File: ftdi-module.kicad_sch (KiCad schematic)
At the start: 60 parts, among them U1 AP62301_TSOT, U2 FT4232H_VQFN, U3 AP62301_TSOT, Y1 Resonator_12MHz_ABM8G

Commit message: Implement changes suggested in schematic review
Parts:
- removed C15, C17, C19, C6, C9: C_100n_0402, antmicro-footprints:C_0402_1005Metric, symbol antmicroCapacitors0402:C_100n_0402
- removed C2, C4: C_4u7_0402, antmicro-footprints:C_0402_1005Metric, symbol antmicroCapacitors0402:C_4u7_0402
- removed FB1, FB2: FB_600Z_0.5A_Murata-BLM18AG_0603, antmicro-footprints:FB_0603_1608Metric, symbol antmicroFerriteBeadsandChips:FB_600Z_0.5A_Murata-BLM18AG_0603
- removed R15: R_33k2_0402, antmicro-footprints:R_0402_1005Metric, symbol antmicroResistors0402:R_33k2_0402
- removed R16, R7: R_10k_0402, antmicro-footprints:R_0402_1005Metric, symbol antmicroResistors0402:R_10k_0402
- removed R6: R_52k3_0402, antmicro-footprints:R_0402_1005Metric, symbol antmicroResistors0402:R_52k3_0402
- removed TP6: TP_1mm_SMD, antmicro-footprints:TP_SMD_1mm, symbol antmicroTestPoints:TP_1mm_SMD
- added C?: C_3u3_0402, antmicro-footprints:C_0402_1005Metric, symbol antmicroCapacitors0402:C_3u3_0402
- added C? (x2): C_100n_0402, antmicro-footprints:C_0402_1005Metric, symbol antmicroCapacitors0402:C_100n_0402
- added C? (x2): C_4u7_0402, antmicro-footprints:C_0402_1005Metric, symbol antmicroCapacitors0402:C_4u7_0402
- added FB? (x2): FB_600Z_0.5A_Murata-BLM18AG_0603, antmicro-footprints:FB_0603_1608Metric, symbol antmicroFerriteBeadsandChips:FB_600Z_0.5A_Murata-BLM18AG_0603
- added R? (x2): R_0R_0402, antmicro-footprints:R_0402_1005Metric, symbol antmicroResistors0402:R_0R_0402
- added R?: R_6k34_0402, antmicro-footprints:R_0402_1005Metric, symbol antmicroResistors0402:R_6k34_0402
- added R? (x2): R_2k_0402, antmicro-footprints:R_0402_1005Metric, symbol antmicroResistors0402:R_2k_0402
- added R?: R_10k7_0402, antmicro-footprints:R_0402_1005Metric, symbol antmicroResistors0402:R_10k7_0402
- C12, R17, R18, R9: DNP (none) -> DNP
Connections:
- net +3V3: now also FB?.1, FB?.1
- net 1V8_FT: now also C?.2
- net FTDI_VPHY: now also C?.2, C?.2, FB?.2
- net FTDI_VPLL: now also C?.2, C?.2, FB?.2
- net GND: now also C?.1, C?.1, C?.1, C?.1, C?.1, R?.2, R?.2
- net SCL: now also R?.2; no longer U2.12 (ADBUS0)
- net SDA: now also R?.2; no longer U2.14 (ADBUS2)
- net at U3.4 (FB): now also R?.1, R?.1
- net at C22.2, C23.2, FB4.1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: now also R?.2
- net at C10.2, C11.2, FB3.1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: now also R?.2
- net at U1.4 (FB): now also R?.1, R?.1
- net SDA_FTDI_2: no longer names the net of R9.1, U2.13 (ADBUS1)
- net USB_D+ renamed USB_BACKPLANE_D+
- net USB_D- renamed USB_BACKPLANE_D-
- net WP: no longer names the net of U2.15 (ADBUS3)
- new net: R?.1, U2.12 (ADBUS0)
- new net: R?.1, U2.14 (ADBUS2)
- no-connect marks 32 -> 33
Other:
- note added: "Values for feedback resitors have been divided by 5 (comparing to datasheet) to eliminate converter failure caused by accidential touch"
- company: (none) -> Antmicro Ltd
- moved on the sheet: C1, C10, C11, C12, C14, C16, C18, C20, C21, C22, C23, C5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

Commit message: 2nd part of review changes
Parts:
- added C15, C17: C_100n_0402, antmicro-footprints:C_0402_1005Metric, symbol antmicroCapacitors0402:C_100n_0402
- C12: DNP DNP -> (none)
- gave numbers to parts that had none: 13
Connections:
- net 1V8_FT: now also C15.2, C17.2
- net GND: now also C15.1, C17.1
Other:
- moved on the sheet: C19

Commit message: Cleaning ERC on schematic
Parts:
- removed FB3, FB4: BLM21SN300SZ1D, antmicro-footprints:FB_0805_2012Metric, symbol antmicroFerriteBeadsandChips:BLM21SN300SZ1D
- added FB3, FB4: FB_30Z_8.5A_Murata-BLM21SN_0805, antmicro-footprints:FB_0805_2012Metric, symbol antmicroFerriteBeadsandChips:FB_30Z_8.5A_Murata-BLM21SN_0805
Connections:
- net +3V3: now also FB4.2
- net +5V: now also FB3.2
- net at C22.2, C23.2, L2.2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: now also FB4.1
- net at C10.2, C11.2, L1.2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: now also FB3.1

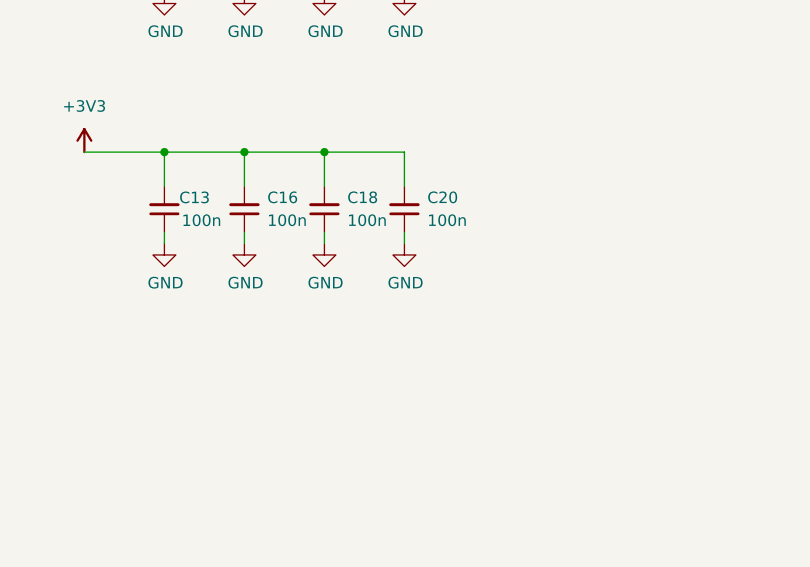
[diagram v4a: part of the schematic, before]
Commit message: Fix possible ERC errors
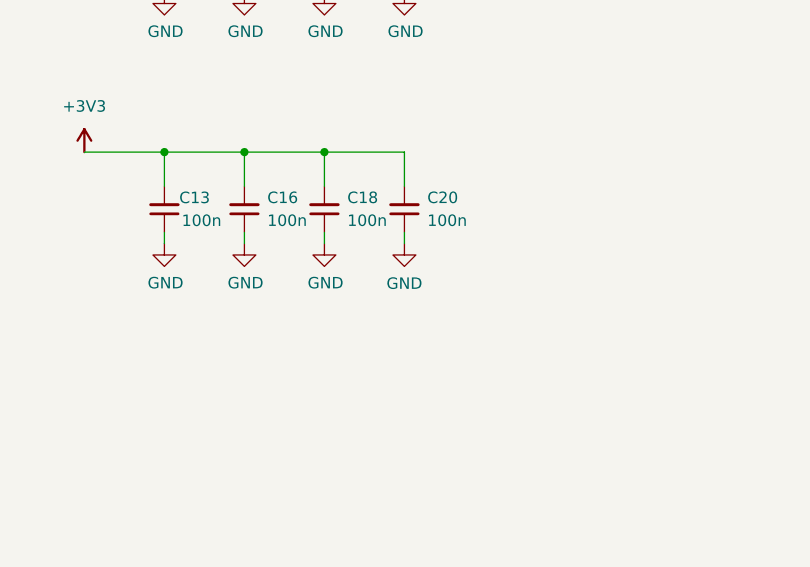
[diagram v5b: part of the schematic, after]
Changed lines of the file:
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@@
     (pin "2")
   )
-  (symbol (lib_id "antmicropower:GND") (at 237.49 133.35 0) (unit 1)
+  (symbol (lib_name "GND_4") (lib_id "antmicropower:GND") (at 237.49 133.35 0) (unit 1)
     (in_bom yes) (on_board yes)
-    (property "Reference" "#PWR035" (id 0) (at 237.49 139.7 0)
-      (effects (font (size 1.27 1.27)) hide)
+    (property "Reference" "#PWR0416" (id 0) (at 246.38 135.89 0)
+      (effects (font (size 1.27 1.27) (thickness 0.15)) (justify left bottom) hide)
     )
-    (property "Value" "GND" (id 1) (at 237.617 137.7442 0))
-    (property "Footprint" "" (id 2) (at 237.49 133.35 0)
-      (effects (font (size 1.27 1.27)) hide)
+    (property "Value" "GND" (id 1) (at 237.49 137.795 0)
+      (effects (font (size 1.27 1.27) (thickness 0.15)))
     )
-    (property "Datasheet" "" (id 3) (at 237.49 133.35 0)
-      (effects (font (size 1.27 1.27)) hide)
+    (property "Footprint" "" (id 2) (at 246.38 140.97 0)
+      (effects (font (size 1.27 1.27) (thickness 0.15)) (justify left bottom) hide)
+    )
+    (property "Datasheet" "" (id 3) (at 246.38 146.05 0)
+      (effects (font (size 1.27 1.27) (thickness 0.15)) (justify left bottom) hide)
+    )
+    (property "Author" "Antmicro" (id 4) (at 246.38 140.97 0)
+      (effects (font (size 1.27 1.27) (thickness 0.15)) (justify left bottom) hide)
+    )
+    (property "License" "Apache-2.0" (id 5) (at 246.38 143.51 0)
+      (effects (font (size 1.27 1.27) (thickness 0.15)) (justify left bottom) hide)
     )
     (pin "1")

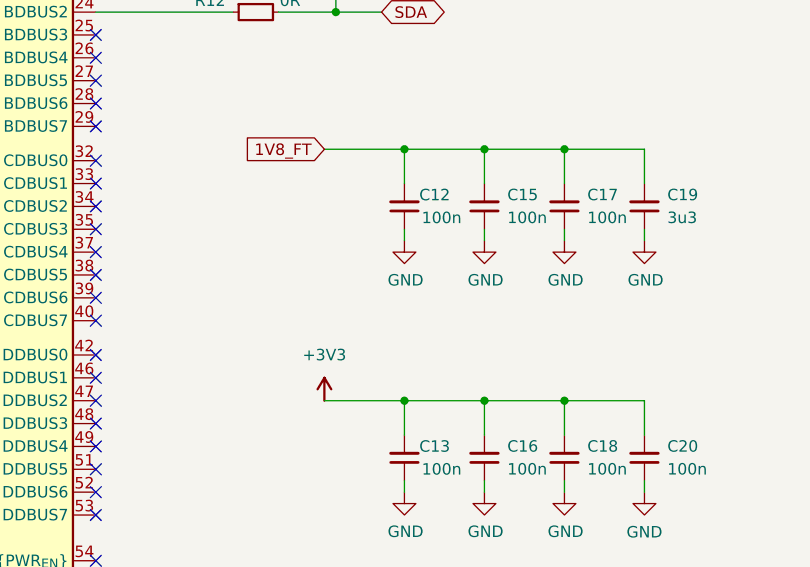
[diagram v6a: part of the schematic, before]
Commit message: Fix ERC errors
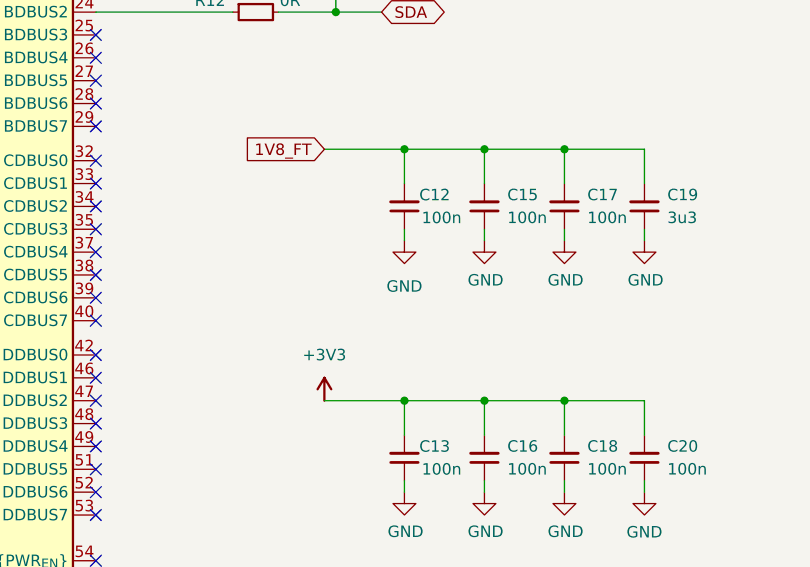
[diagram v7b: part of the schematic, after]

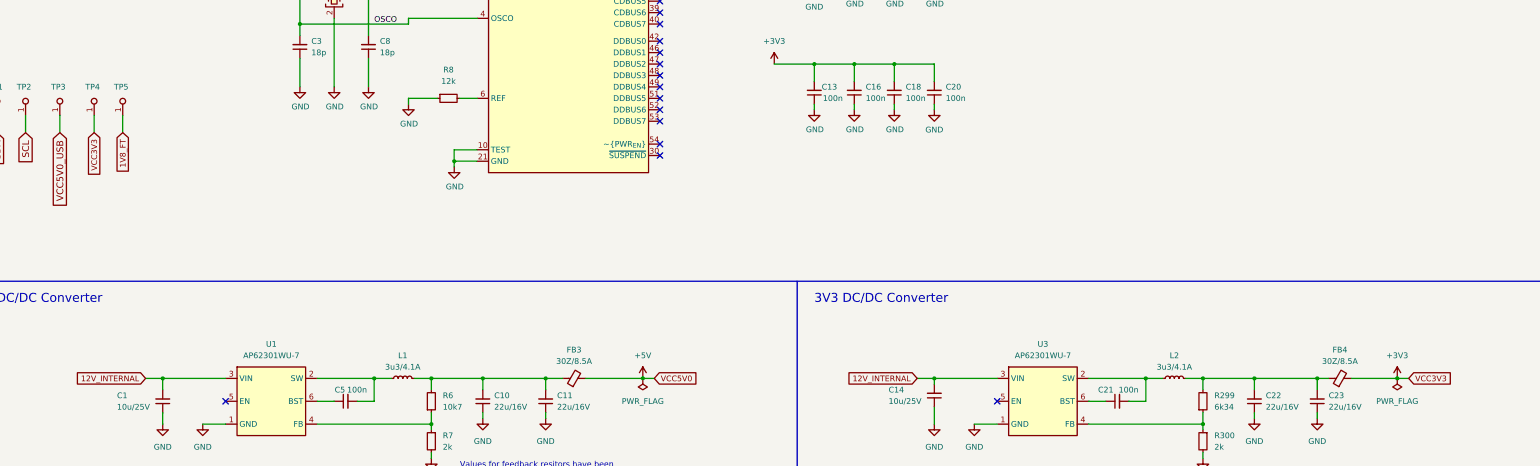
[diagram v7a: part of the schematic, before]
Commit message: Fix ESD diode symbol and GPU connector symbol
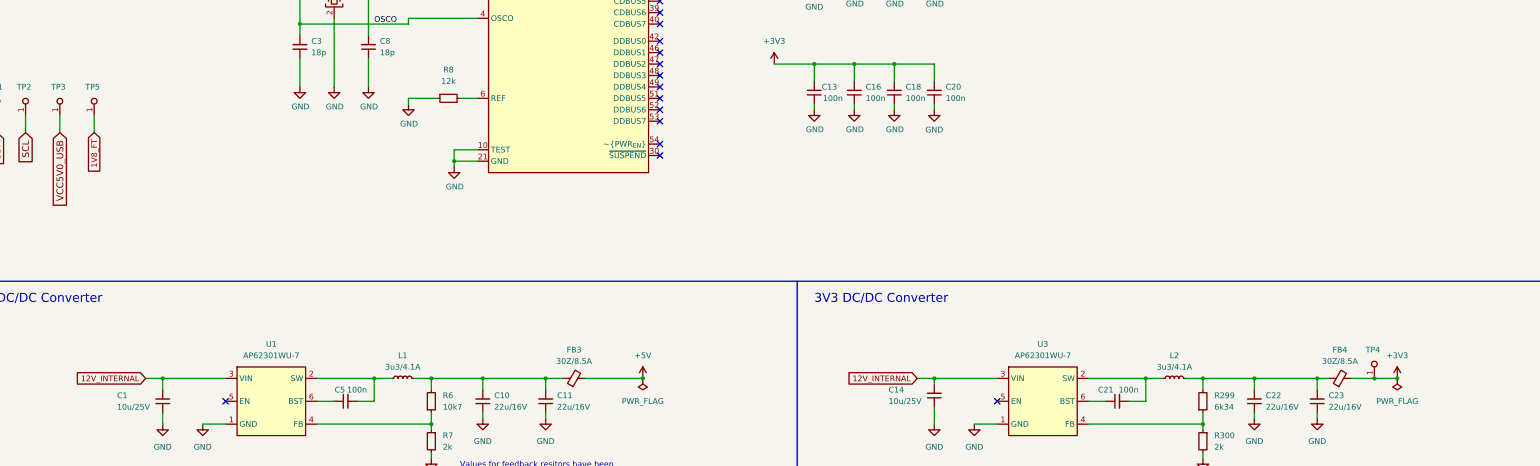
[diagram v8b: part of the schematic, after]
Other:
- moved on the sheet: TP4, TP5
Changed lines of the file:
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@@
   (junction (at 125.73 203.2) (diameter 0) (color 0 0 0 0)
   )
+  (junction (at 335.28 193.04) (diameter 0) (color 0 0 0 0)
+  )
   (junction (at 297.18 193.04) (diameter 0) (color 0 0 0 0)
   )
@@
     (stroke (width 0) (type default) (color 0 0 0 0))
   )
-  (wire (pts (xy 50.8 138.43) (xy 50.8 134.62))
+  (wire (pts (xy 335.28 193.04) (xy 340.36 193.04))
     (stroke (width 0) (type default) (color 0 0 0 0))
   )
@@
     (stroke (width 0) (type default) (color 0 0 0 0))
   )
-  (wire (pts (xy 340.36 193.04) (xy 342.9 193.04))
-    (stroke (width 0) (type default) (color 0 0 0 0))
-  )
   (wire (pts (xy 210.82 95.25) (xy 219.71 95.25))
     (stroke (width 0) (type default) (color 0 0 0 0))
@@
     (stroke (width 0) (type default) (color 0 0 0 0))
   )
-  (wire (pts (xy 57.15 138.43) (xy 57.15 134.62))
+  (wire (pts (xy 50.8 138.43) (xy 50.8 134.62))
     (stroke (width 0) (type default) (color 0 0 0 0))
   )
@@
     (stroke (width 0) (type default) (color 0 0 0 0))
   )
-  (wire (pts (xy 172.72 193.04) (xy 175.26 193.04))
-    (stroke (width 0) (type default) (color 0 0 0 0))
-  )
   (wire (pts (xy 58.42 62.23) (xy 58.42 63.5))
     (stroke (width 0) (type default) (color 0 0 0 0))
@@
     (stroke (width 0) (type default) (color 0 0 0 0))
   )
-  (wire (pts (xy 330.2 193.04) (xy 340.36 193.04))
+  (wire (pts (xy 330.2 193.04) (xy 335.28 193.04))
     (stroke (width 0) (type default) (color 0 0 0 0))
   )
@@
     )
   )
-  (global_label "VCC3V3" (shape input) (at 50.8 138.43 270) (fields_autoplaced)
-    (effects (font (size 1.27 1.27)) (justify right))
-    (property "Intersheet References" "${INTERSHEET_REFS}" (id 0) (at 260.35 204.47 0)
-      (effects (font (size 1.27 1.27)) hide)
-    )
-  )
-  (global_label "1V8_FT" (shape input) (at 57.15 138.43 270) (fields_autoplaced)
+  (global_label "1V8_FT" (shape input) (at 50.8 138.43 270) (fields_autoplaced)
     (effects (font (size 1.27 1.27)) (justify right))
-    (property "Intersheet References" "${INTERSHEET_REFS}" (id 0) (at -118.11 264.16 0)
+    (property "Intersheet References" "${INTERSHEET_REFS}" (id 0) (at -124.46 264.16 0)
       (effects (font (size 1.27 1.27)) hide)
     )
@@
     )
   )
-  (global_label "VCC3V3" (shape input) (at 342.9 193.04 0) (fields_autoplaced)
-    (effects (font (size 1.27 1.27)) (justify left))
-    (property "Intersheet References" "${INTERSHEET_REFS}" (id 0) (at 193.675 91.44 0)
-      (effects (font (size 1.27 1.27)) hide)
-    )
-  )
   (global_label "SDA" (shape bidirectional) (at 236.22 55.88 180) (fields_autoplaced)
     (effects (font (size 1.27 1.27)) (justify right))
@@
     )
   )
-  (global_label "VCC5V0" (shape input) (at 175.26 193.04 0) (fields_autoplaced)
-    (effects (font (size 1.27 1.27)) (justify left))
-    (property "Intersheet References" "${INTERSHEET_REFS}" (id 0) (at 184.7204 192.9606 0)
-      (effects (font (size 1.27 1.27)) (justify left) hide)
-    )
-  )
   (global_label "SDA" (shape bidirectional) (at 293.37 59.69 180) (fields_autoplaced)
     (effects (font (size 1.27 1.27)) (justify right))
@@
     (pin "2")
   )
-  (symbol (lib_id "antmicroTestPoints:TP_1mm_SMD") (at 57.15 134.62 90) (unit 1)
+  (symbol (lib_id "antmicroTestPoints:TP_1mm_SMD") (at 50.8 134.62 90) (unit 1)
     (in_bom yes) (on_board yes)
-    (property "Reference" "TP5" (id 0) (at 58.42 128.27 90)
+    (property "Reference" "TP5" (id 0) (at 52.07 128.27 90)
       (effects (font (size 1.27 1.27) (thickness 0.15)) (justify left))
     )
-    (property "Value" "TP_1mm_SMD" (id 1) (at 64.77 119.38 0)
+    (property "Value" "TP_1mm_SMD" (id 1) (at 58.42 119.38 0)
       (effects (font (size 1.27 1.27) (thickness 0.15)) (justify left bottom) hide)
     )
-    (property "Footprint" "antmicro-footprints:TP_SMD_1mm" (id 2) (at 67.31 119.38 0)
+    (property "Footprint" "antmicro-footprints:TP_SMD_1mm" (id 2) (at 60.96 119.38 0)
       (effects (font (size 1.27 1.27) (thickness 0.15)) (justify left bottom) hide)
     )
-    (property "Datasheet" "" (id 3) (at 69.85 116.84 0)
+    (property "Datasheet" "" (id 3) (at 63.5 116.84 0)
       (effects (font (size 1.27 1.27) (thickness 0.15)) (justify left bottom) hide)
     )
-    (property "MPN" "" (id 4) (at 57.15 134.62 0)
+    (property "MPN" "" (id 4) (at 50.8 134.62 0)
       (effects (font (size 1.27 1.27)) hide)
     )
-    (property "Manufacturer" "" (id 5) (at 57.15 134.62 0)
+    (property "Manufacturer" "" (id 5) (at 50.8 134.62 0)
       (effects (font (size 1.27 1.27)) hide)
     )
-    (property "Author" "Antmicro" (id 6) (at 72.39 119.38 0)
+    (property "Author" "Antmicro" (id 6) (at 66.04 119.38 0)
       (effects (font (size 1.27 1.27) (thickness 0.15)) (justify left bottom) hide)
     )
-    (property "License" "Apache-2.0" (id 7) (at 74.93 119.38 0)
+    (property "License" "Apache-2.0" (id 7) (at 68.58 119.38 0)
       (effects (font (size 1.27 1.27) (thickness 0.15)) (justify left bottom) hide)
     )
@@
     (pin "1")
   )
-  (symbol (lib_id "antmicroTestPoints:TP_1mm_SMD") (at 50.8 134.62 90) (unit 1)
+  (symbol (lib_id "antmicroTestPoints:TP_1mm_SMD") (at 335.28 193.04 90) (unit 1)
     (in_bom yes) (on_board yes)
-    (property "Reference" "TP4" (id 0) (at 52.07 128.27 90)
+    (property "Reference" "TP4" (id 0) (at 336.55 186.69 90)
       (effects (font (size 1.27 1.27) (thickness 0.15)) (justify left))
     )
-    (property "Value" "TP_1mm_SMD" (id 1) (at 58.42 119.38 0)
+    (property "Value" "TP_1mm_SMD" (id 1) (at 342.9 177.8 0)
       (effects (font (size 1.27 1.27) (thickness 0.15)) (justify left bottom) hide)
     )
-    (property "Footprint" "antmicro-footprints:TP_SMD_1mm" (id 2) (at 60.96 119.38 0)
+    (property "Footprint" "antmicro-footprints:TP_SMD_1mm" (id 2) (at 345.44 177.8 0)
       (effects (font (size 1.27 1.27) (thickness 0.15)) (justify left bottom) hide)
     )
-    (property "Datasheet" "" (id 3) (at 63.5 116.84 0)
+    (property "Datasheet" "" (id 3) (at 347.98 175.26 0)
       (effects (font (size 1.27 1.27) (thickness 0.15)) (justify left bottom) hide)
     )
-    (property "MPN" "" (id 4) (at 50.8 134.62 0)
+    (property "MPN" "" (id 4) (at 335.28 193.04 0)
       (effects (font (size 1.27 1.27)) hide)
     )
-    (property "Manufacturer" "" (id 5) (at 50.8 134.62 0)
+    (property "Manufacturer" "" (id 5) (at 335.28 193.04 0)
       (effects (font (size 1.27 1.27)) hide)
     )
-    (property "Author" "Antmicro" (id 6) (at 66.04 119.38 0)
+    (property "Author" "Antmicro" (id 6) (at 350.52 177.8 0)
       (effects (font (size 1.27 1.27) (thickness 0.15)) (justify left bottom) hide)
     )
-    (property "License" "Apache-2.0" (id 7) (at 68.58 119.38 0)
+    (property "License" "Apache-2.0" (id 7) (at 353.06 177.8 0)
       (effects (font (size 1.27 1.27) (thickness 0.15)) (justify left bottom) hide)
     )
